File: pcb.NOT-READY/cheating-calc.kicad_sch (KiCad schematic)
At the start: 22 parts, among them J1 Conn_01x04, Q1 MMBF170, Q2 MMBF170, SW1 MK-12C02-G020, U1 MOUDLE-SEEEDUINO-XIAO-ESP32C3, U2 SE5218ALG-LF, U3 USB-111HF-B-CU, U4 ESP32-C3-WROOM-02-N4(4MB), U5 BL8071CLBTR33, U6 XC6210B332MR_C3021084

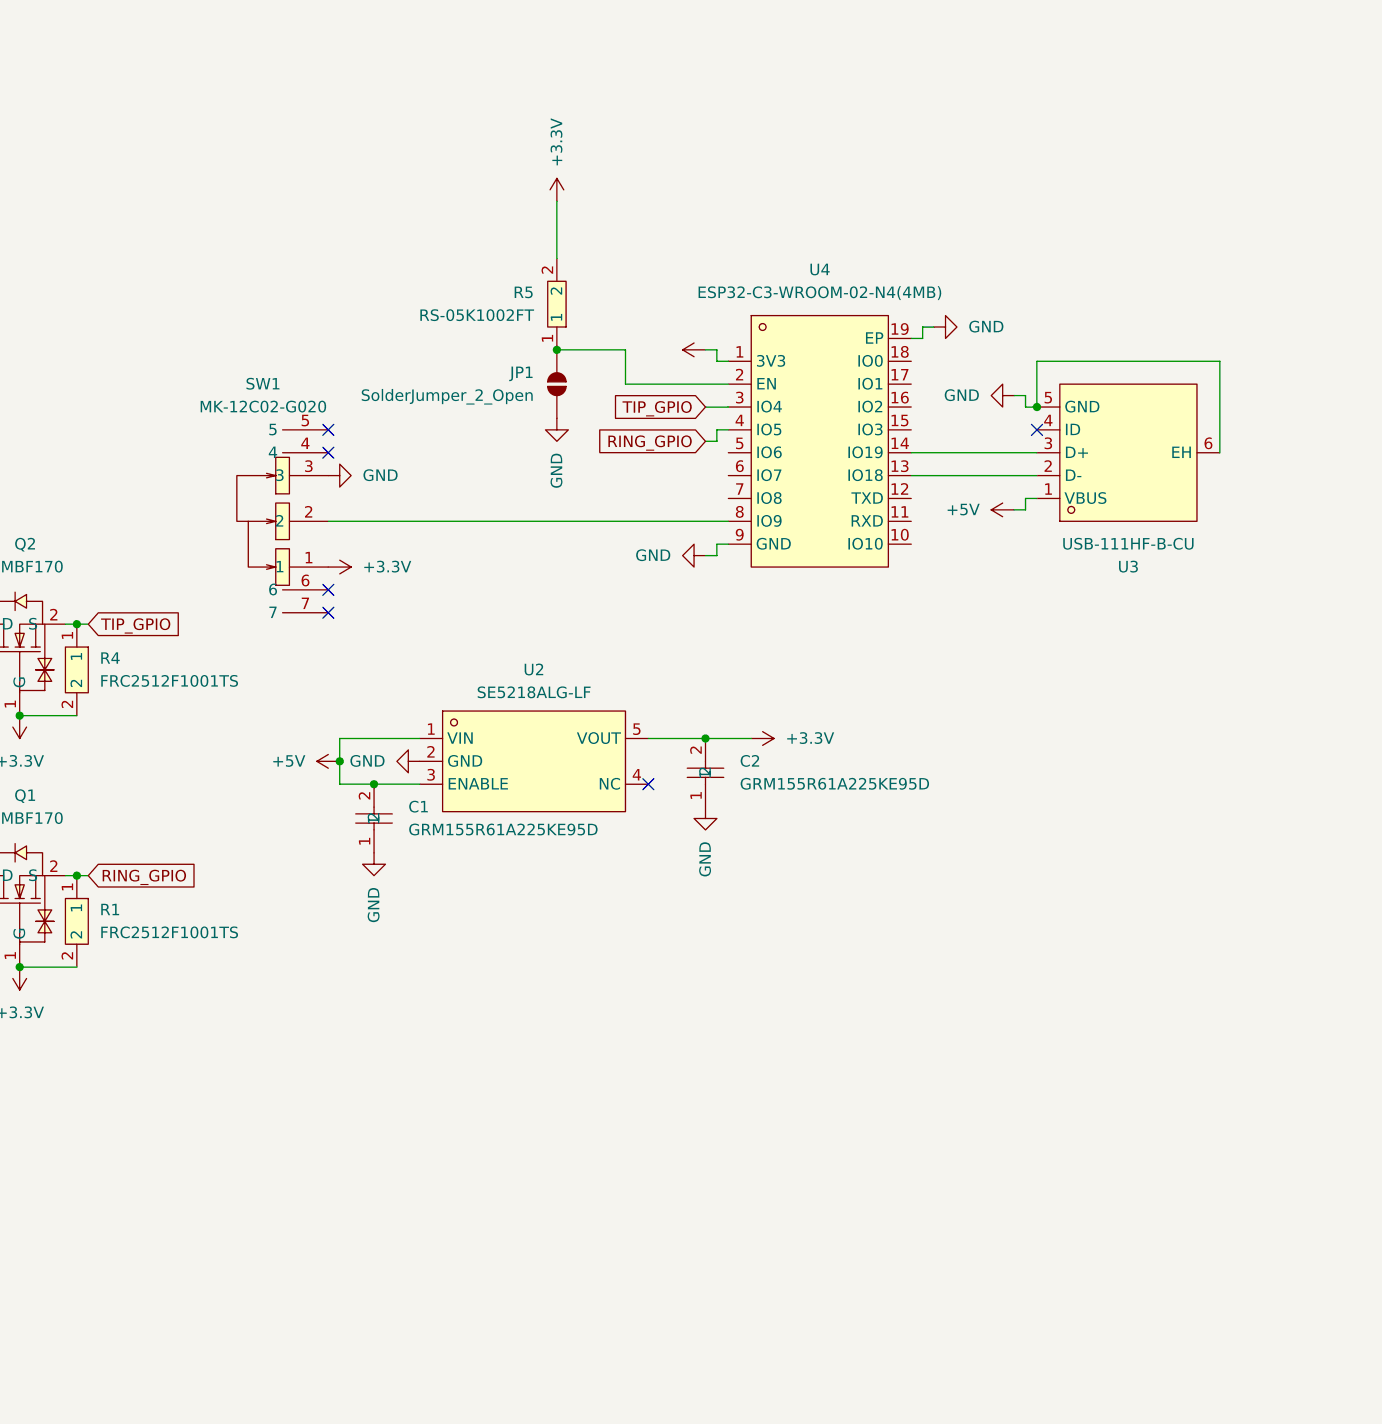
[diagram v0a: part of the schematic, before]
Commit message: change layout parts and esp32 module choice for space savings
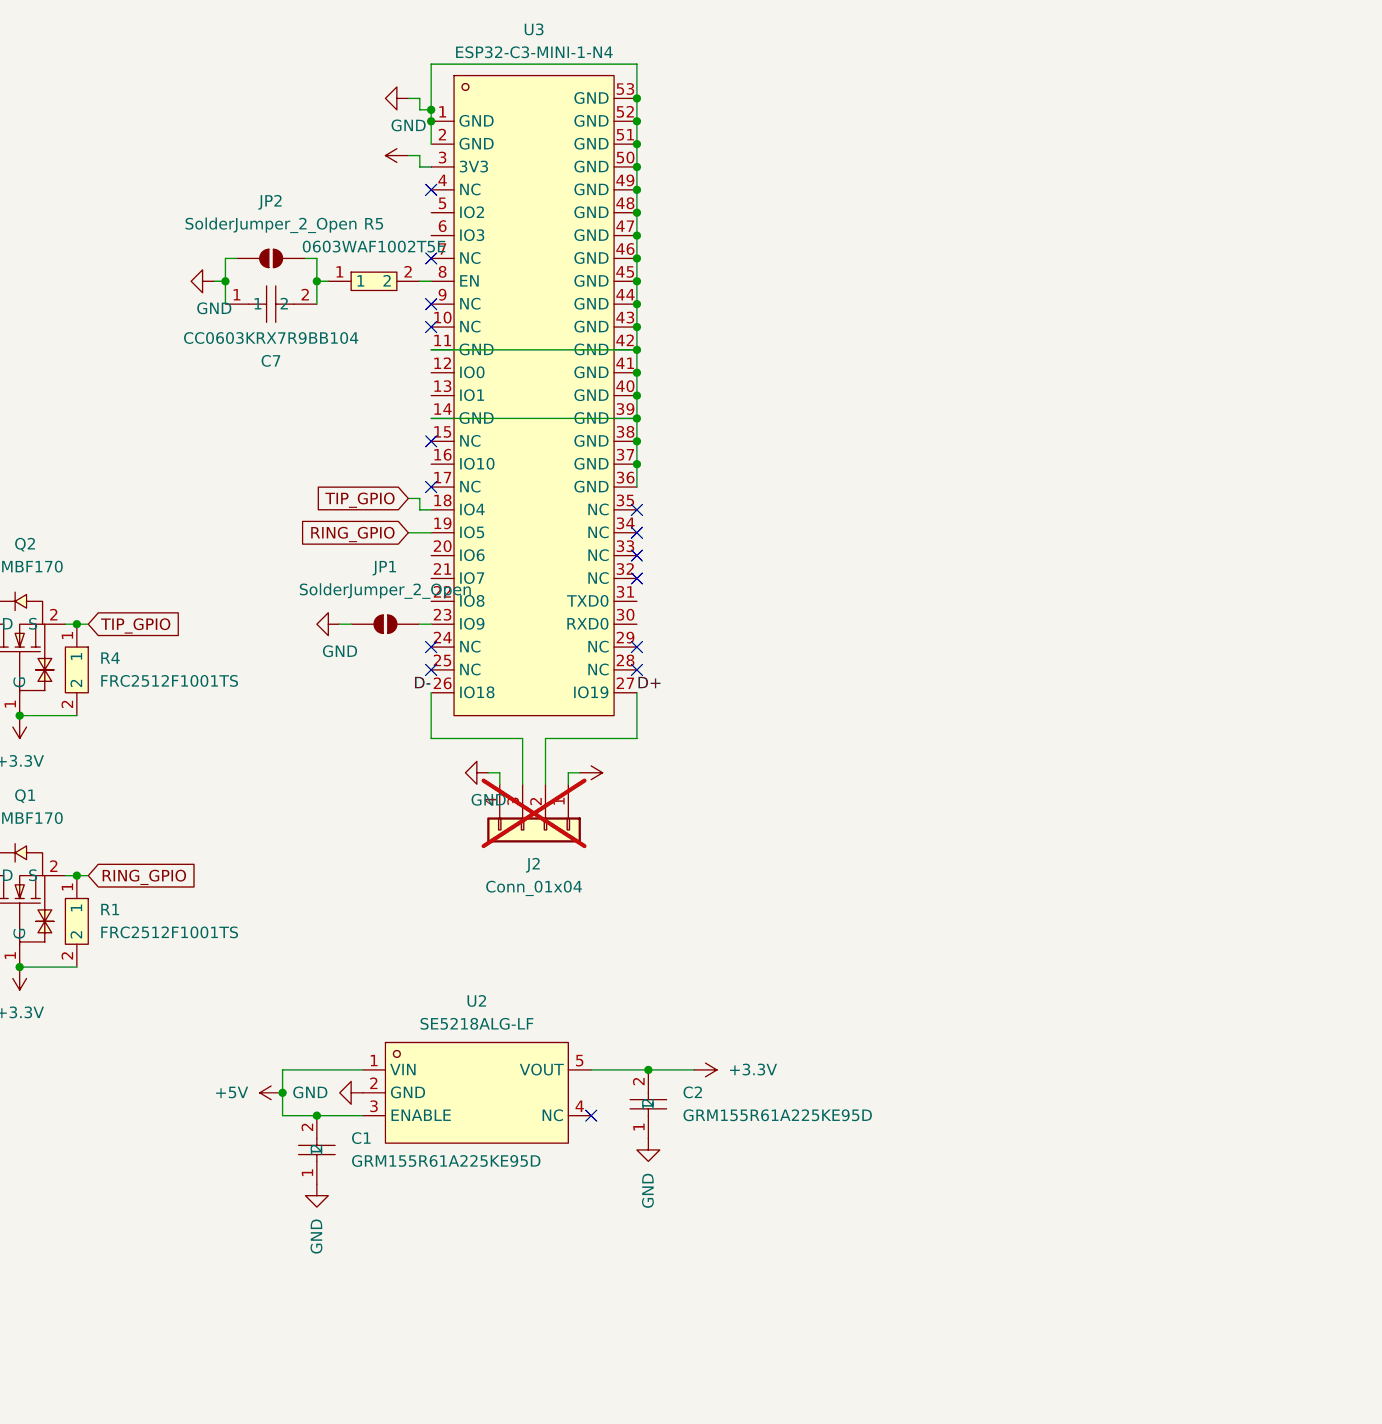
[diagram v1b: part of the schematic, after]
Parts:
- removed R5: RS-05K1002FT, easyeda2kicad:R0805, symbol easyeda2kicad:RS-05K1002FT
- removed SW1: MK-12C02-G020, easyeda2kicad:SW-SMD_MK-12C02-G020, symbol easyeda2kicad:MK-12C02-G020
- removed U3: USB-111HF-B-CU, easyeda2kicad:MICRO-USB-SMD_HOOYA_USB-111HF-B-CU, symbol easyeda2kicad:USB-111HF-B-CU
- removed U4: ESP32-C3-WROOM-02-N4(4MB), easyeda2kicad:BULETM-SMD_ESPRESSIF_ESP32-C3-WROOM-02-N4-4MB, symbol easyeda2kicad:ESP32-C3-WROOM-02-N4(4MB)
- added C7: CC0603KRX7R9BB104, easyeda2kicad:C0603, symbol easyeda2kicad:CC0603KRX7R9BB104
- added J2: Conn_01x04, Connector_PinHeader_2.54mm:PinHeader_1x04_P2.54mm_Vertical, symbol Connector_Generic:Conn_01x04
- added JP2: SolderJumper_2_Open, Jumper:SolderJumper-2_P1.3mm_Open_RoundedPad1.0x1.5mm, symbol Jumper:SolderJumper_2_Open
- added R5: 0603WAF1002T5E, easyeda2kicad:R0603, symbol easyeda2kicad:0603WAF1002T5E
- added U3: ESP32-C3-MINI-1-N4, easyeda2kicad:WIFIM-SMD_ESP32-C3-MINI-1, symbol easyeda2kicad:ESP32-C3-MINI-1-N4
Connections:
- net +3.3V: now also U3.3 (3V3)
- net +5V: now also J2.1 (Pin_1)
- net GND: now also C7.1, J2.4 (Pin_4), JP2.1 (A), U3.1 (GND), U3.11 (GND), U3.14 (GND), U3.2 (GND), U3.36 (GND), U3.37 (GND), U3.38 (GND), U3.39 (GND), U3.40 (GND), U3.41 (GND), U3.42 (GND), U3.43 (GND), U3.44 (GND), U3.45 (GND), U3.46 (GND), U3.47 (GND), U3.48 (GND), U3.49 (GND), U3.50 (GND), U3.51 (GND), U3.52 (GND), U3.53 (GND)
- net RING_GPIO: now also U3.19 (IO5)
- net TIP_GPIO: now also U3.18 (IO4)
- net at JP1.2 (B): now also U3.23 (IO9)
- new net: C7.2, JP2.2 (B), R5.1
- new net: R5.2, U3.8 (EN)
- new net D+: J2.2 (Pin_2), U3.27 (IO19)
- new net D-: J2.3 (Pin_3), U3.26 (IO18)
- no-connect marks 7 -> 16
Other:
- moved on the sheet: C1, C2, U2

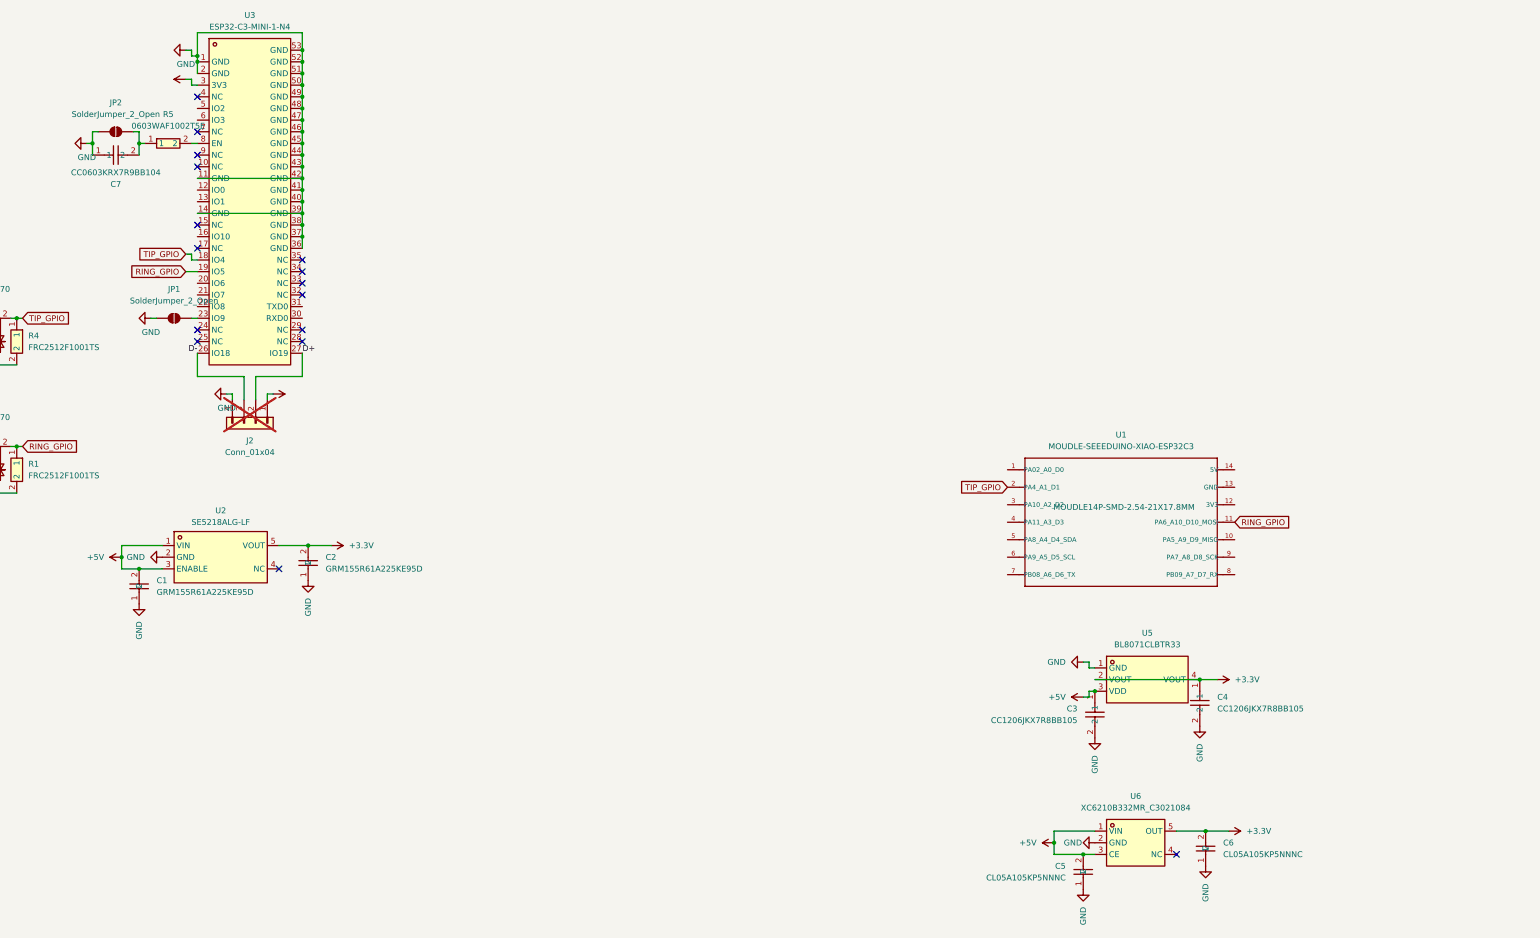
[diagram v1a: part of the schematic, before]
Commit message: update LDO regulator to be a genuine TI (and add redundency for other versions in schem)
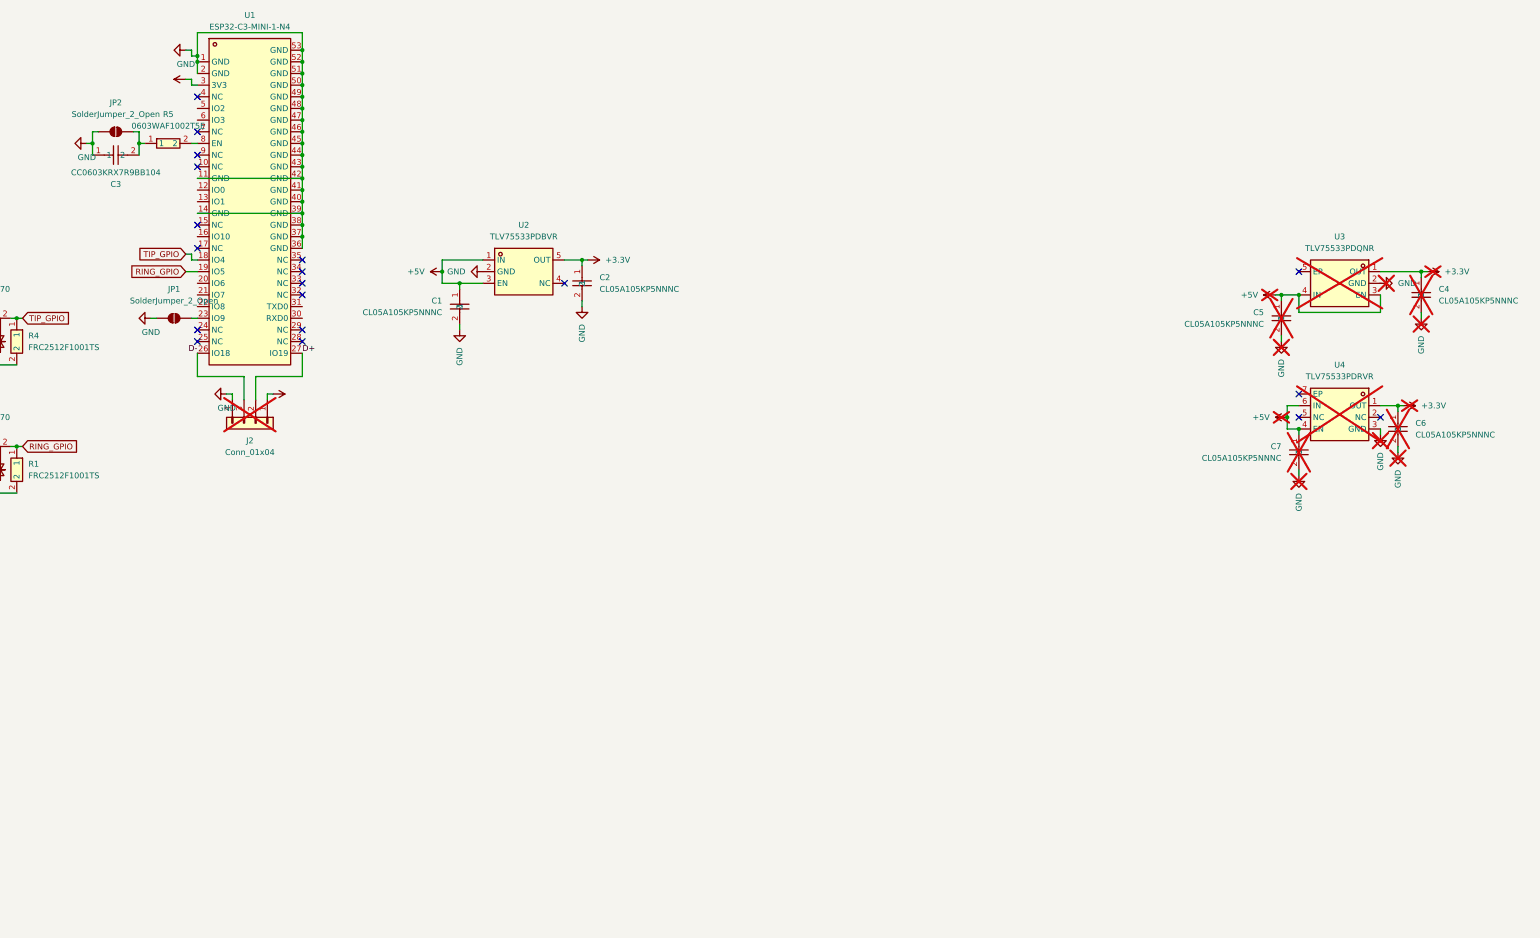
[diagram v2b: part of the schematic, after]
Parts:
- removed C1, C2: GRM155R61A225KE95D, easyeda2kicad:C0402, symbol easyeda2kicad:GRM155R61A225KE95D
- removed C3, C4: CC1206JKX7R8BB105, easyeda2kicad:C1206, symbol easyeda2kicad:CC1206JKX7R8BB105
- removed U1: MOUDLE-SEEEDUINO-XIAO-ESP32C3, MOUDLE14P-SMD-2.54-21X17.8MM, symbol XIAO:MOUDLE-SEEEDUINO-XIAO-ESP32C3
- removed U2: SE5218ALG-LF, easyeda2kicad:SOT-23-5_L3.0-W1.7-P0.95-LS2.8-BR, symbol easyeda2kicad:SE5218ALG-LF
- removed U5: BL8071CLBTR33, easyeda2kicad:SOT-223_L6.5-W3.5-P2.30-LS7.0-BR, symbol easyeda2kicad:BL8071CLBTR33
- removed U6: XC6210B332MR_C3021084, easyeda2kicad:SOT-23-5_L2.9-W1.6-P0.95-LS2.8-BR, symbol easyeda2kicad:XC6210B332MR_C3021084
- added C1, C2, C4, C7: CL05A105KP5NNNC, easyeda2kicad:C0402, symbol easyeda2kicad:CL05A105KP5NNNC
- added U2: TLV75533PDBVR, easyeda2kicad:SOT-23-5_L3.0-W1.7-P0.95-LS2.8-BR, symbol easyeda2kicad:TLV75533PDBVR
- added U3: TLV75533PDQNR, easyeda2kicad:X2SON-4_L1.0-W1.0-P0.65-TL-EP, symbol easyeda2kicad:TLV75533PDQNR
- added U4: TLV75533PDRVR, easyeda2kicad:WSON-6_L2.0-W2.0-P0.65-TL-EP, symbol easyeda2kicad:TLV75533PDRVR
- C5, C6: now not fitted; now left out of the parts list
- renumbered C7 to C3, U3 to U1
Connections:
- net +3.3V: now also C6.1, C2.1, C4.1, U2.5 (OUT), U3.1 (OUT), U4.1 (OUT); no longer C6.2
- net +5V: now also C5.1, C1.1, C7.1, U2.1 (IN), U2.3 (EN), U3.3 (EN), U3.4 (IN), U4.4 (EN), U4.6 (IN); no longer C5.2
- net GND: now also C5.2, C6.2, C1.2, C2.2, C4.2, C7.2, U2.2 (GND), U3.2 (GND), U4.3 (GND); no longer C5.1, C6.1
- no-connect marks 16 -> 19
